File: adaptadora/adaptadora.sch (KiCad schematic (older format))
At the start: 39 parts, among them J1 Conn_Coaxial, J10 Conn_01x02, J11 Conn_Coaxial, J12 Conn_Coaxial, J2 Conn_Coaxial, J3 Conn_Coaxial, J4 Conn_Coaxial, J5 Conn_Coaxial, J6 Conn_01x02, J7 Conn_02x20_Odd_Even, J8 Conn_02x20_Odd_Even, J9 Conn_01x04, U1 LM361MX_NOPB-LM361MX_NOPB, U2 TLV2772IDR

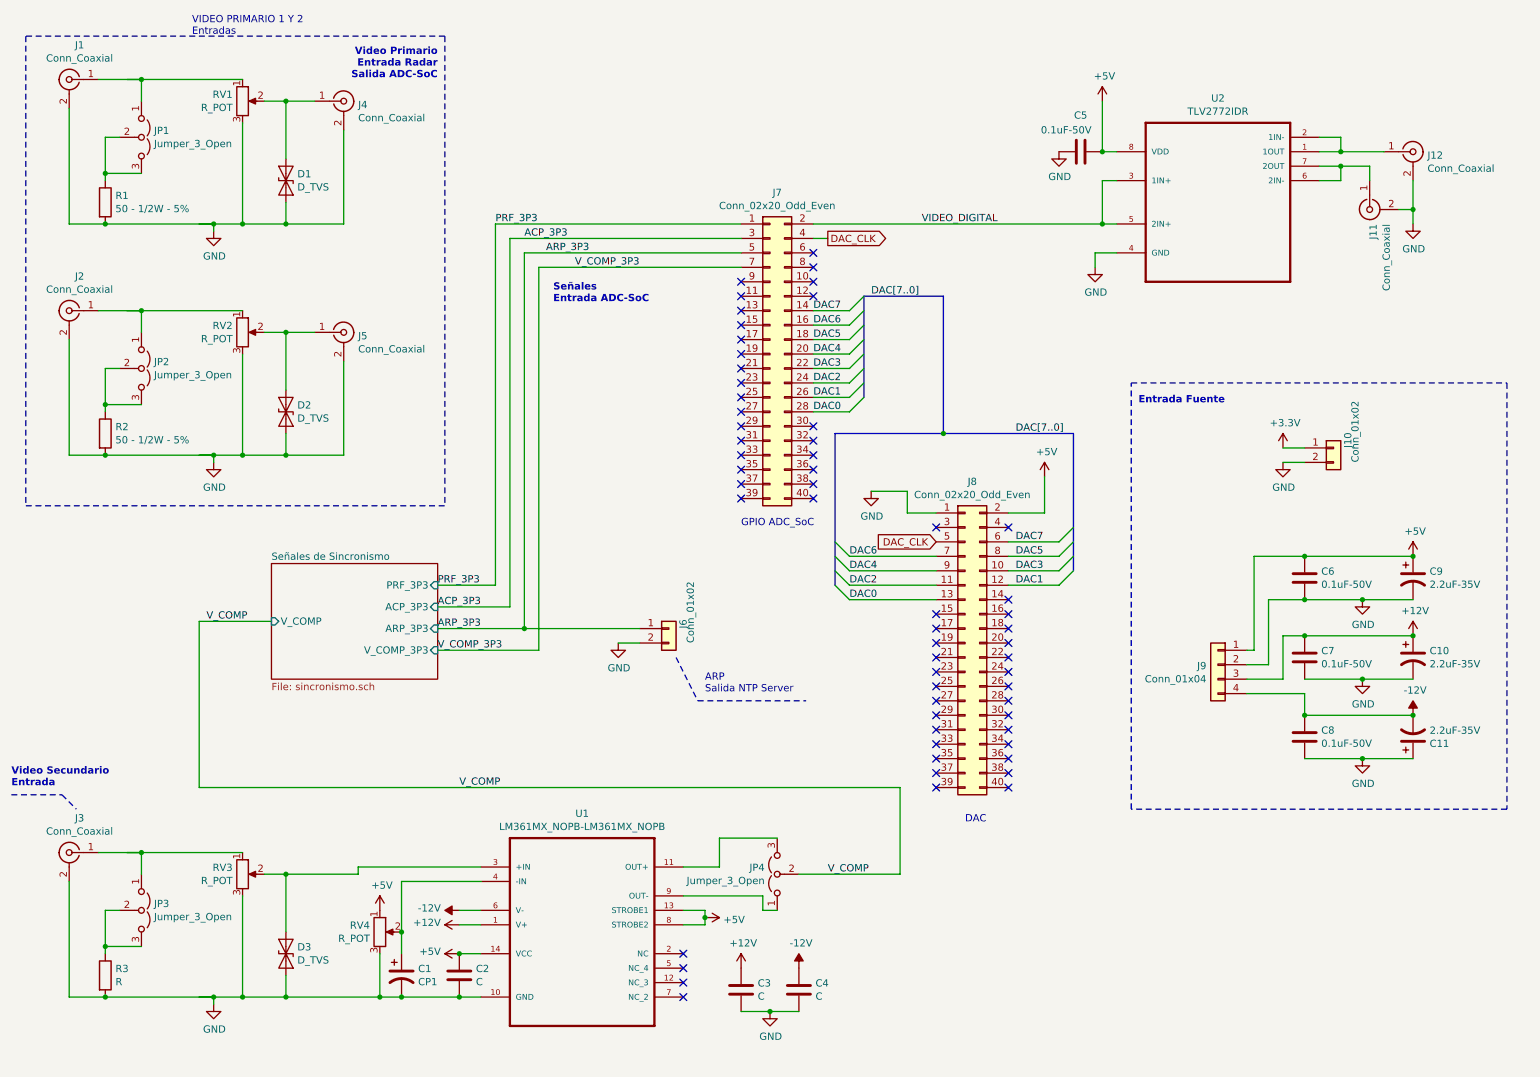
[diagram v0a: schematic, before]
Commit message: esquemático corregido por compañero
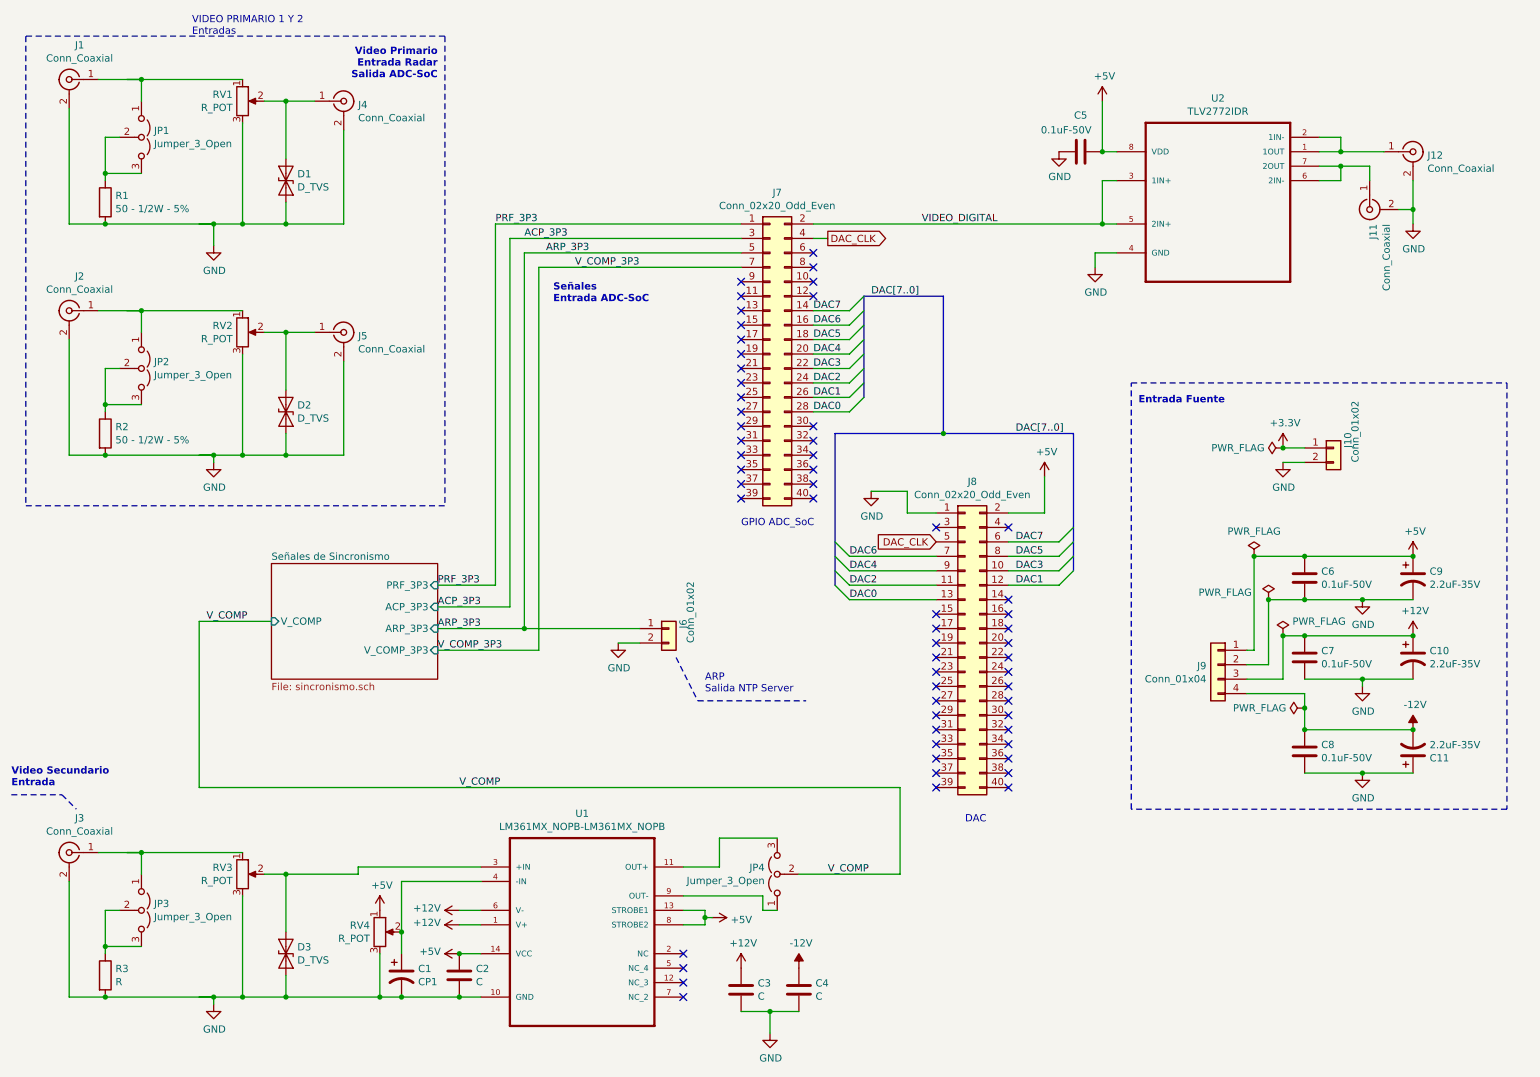
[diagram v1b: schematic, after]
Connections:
- wire segments 172 -> 176
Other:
- moved on the sheet: C11, C8

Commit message: work in progress
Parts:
- removed C1: CP1, symbol Device:CP1
- removed C2, C3, C4: C, symbol Device:C
- removed D3: D_TVS, symbol Device:D_TVS
- removed J3: Conn_Coaxial, symbol Connector:Conn_Coaxial
- removed JP3, JP4: Jumper_3_Open, symbol Jumper:Jumper_3_Open
- removed R3: R, symbol Device:R
- removed RV3, RV4: R_POT, symbol Device:R_POT
- removed U1: LM361MX_NOPB-LM361MX_NOPB, SOIC127P600X175-14N, symbol sincronismo-rescue:LM361MX_NOPB-LM361MX_NOPB
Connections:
- net labels removed: V_COMP
- wire segments 176 -> 124
- no-connect marks 59 -> 55
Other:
- note added: "Video Primario Digital\nSalida a otros equipos"
- note removed: "Video Secundario\nEntrada"
- moved on the sheet: D1, D2, J1, J11, J12, J2, J4, J5, J6, J7, J8, JP1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

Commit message: correcciones implementadas
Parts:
- U2_1: renamed from U2; Campo4 Texas Instruments -> (none); Campo5 Dual 2.7-V High Slew Rate Rail-To-Rail Output Operational A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 -> (none); Campo6 TLV2772IDR -> (none); Campo7 https://www.digikey.com/product-detail/en/texas-instruments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 -> (none); Campo8 SOIC-8 Texas Instruments -> (none); Descripción (inglés) (none) -> Dual 2.7-V High Slew Rate Rail-To-Rail Output Operational A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; Enlace (none) -> https://www.digikey.com/product-detail/en/texas-instruments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; Fabricante (none) -> Texas Instruments; Número de Parte (Digi-Key) (none) -> 296-1902-1-ND
- renumbered C5 to C1, C8 to C2, C11 to C3, C6 to C4, C7 to C5, C9 to C6, C10 to C7, J11 to J10, J12 to J11, J4 to J3, J5 to J4, J7 to J5, J8 to J7, J9 to J8, J10 to J9
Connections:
- wire segments 124 -> 130
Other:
- note added: "Señal de Video Secundario\nSeñal de Sincronismo de Rango\nEntradas ADC-SoC"
- note added: "Señales de sincronismo de Acimut\nEntrada ADC-SoC"
- note added: "U2_X: Amplificadores operacionales\nSalidas duplicadas para otros equipos\nTensión de salida: 5V"
- note removed: "Señales\nEntrada ADC-SoC"
- moved on the sheet: C2, C3, C4, C5, C6, C7, J7, J8, J9

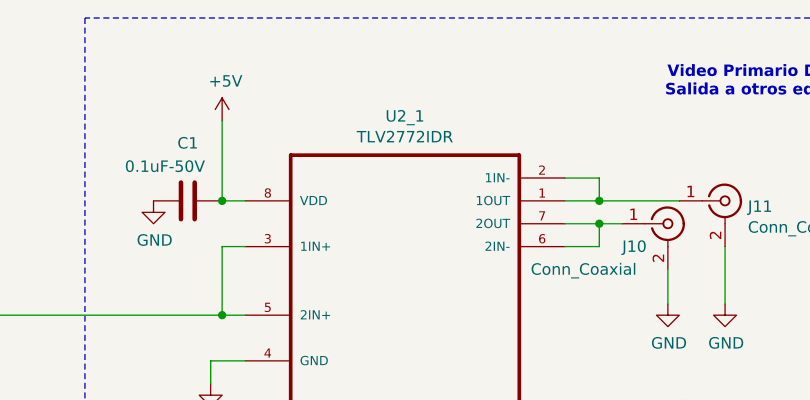
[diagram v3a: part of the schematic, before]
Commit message: se agregan huellas, en progreso
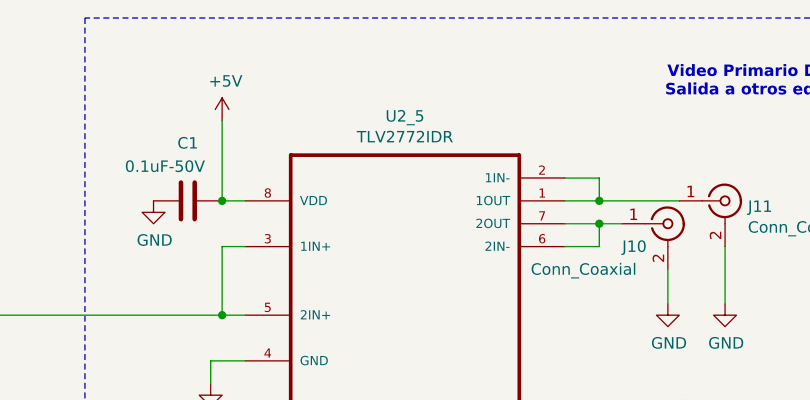
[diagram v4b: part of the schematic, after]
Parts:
- J1, J10, J11, J2, J3, J4: footprint (none) -> Connector_Coaxial:SMA_Amphenol_901-144_Vertical
- renumbered U2_1 to U2_5
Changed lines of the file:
@@
 F 0 "J1" H 1578 4388 50  0000 C CNN
 F 1 "Conn_Coaxial" H 1578 4297 50  0000 C CNN
-F 2 "" H 1650 4150 50  0001 C CNN
+F 2 "Connector_Coaxial:SMA_Amphenol_901-144_Vertical" H 1650 4150 50  0001 C CNN
 F 3 " ~" H 1650 4150 50  0001 C CNN
 	1    1650 4150
@@
 F 0 "J3" H 3650 4275 50  0000 L CNN
 F 1 "Conn_Coaxial" H 3650 4184 50  0000 L CNN
-F 2 "" H 3550 4300 50  0001 C CNN
+F 2 "Connector_Coaxial:SMA_Amphenol_901-144_Vertical" H 3550 4300 50  0001 C CNN
 F 3 " ~" H 3550 4300 50  0001 C CNN
 	1    3550 4300
@@
 F 0 "J2" H 1578 5988 50  0000 C CNN
 F 1 "Conn_Coaxial" H 1578 5897 50  0000 C CNN
-F 2 "" H 1650 5750 50  0001 C CNN
+F 2 "Connector_Coaxial:SMA_Amphenol_901-144_Vertical" H 1650 5750 50  0001 C CNN
 F 3 " ~" H 1650 5750 50  0001 C CNN
 	1    1650 5750
@@
 F 0 "J4" H 3650 5875 50  0000 L CNN
 F 1 "Conn_Coaxial" H 3650 5784 50  0000 L CNN
-F 2 "" H 3550 5900 50  0001 C CNN
+F 2 "Connector_Coaxial:SMA_Amphenol_901-144_Vertical" H 3550 5900 50  0001 C CNN
 F 3 " ~" H 3550 5900 50  0001 C CNN
 	1    3550 5900
@@
 F 0 "J10" H 9900 1400 50  0000 L CNN
 F 1 "Conn_Coaxial" H 9500 1300 50  0000 L CNN
-F 2 "" H 10100 1500 50  0001 C CNN
+F 2 "Connector_Coaxial:SMA_Amphenol_901-144_Vertical" H 10100 1500 50  0001 C CNN
 F 3 " ~" H 10100 1500 50  0001 C CNN
 	1    10100 1500
@@
 F 0 "J11" H 10450 1375 50  0000 L CNN
 F 1 "Conn_Coaxial" H 10450 1284 50  0000 L CNN
-F 2 "" H 10350 1400 50  0001 C CNN
+F 2 "Connector_Coaxial:SMA_Amphenol_901-144_Vertical" H 10350 1400 50  0001 C CNN
 F 3 " ~" H 10350 1400 50  0001 C CNN
 	1    10350 1400
@@
 $EndComp
 $Comp
-L TLV2772IDR:TLV2772IDR U2_1
+L TLV2772IDR:TLV2772IDR U2_5
 U 1 1 5DB05057
 P 8950 1600
-F 0 "U2_1" H 8950 2170 50  0000 C CNN
+F 0 "U2_5" H 8950 2170 50  0000 C CNN
 F 1 "TLV2772IDR" H 8950 2079 50  0000 C CNN
 F 2 "SOIC127P600X175-8N" H 8950 1150 50  0001 L BNN

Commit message: pcb work in progress
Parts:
- C1, C2, C4, C5: footprint (none) -> Capacitor_SMD:C_0805_2012Metric
- C3, C6, C7: footprint (none) -> Capacitor_Tantalum_SMD:CP_EIA-6032-28_Kemet-C
- D1, D2: footprint (none) -> Diode_THT:D_DO-15_P10.16mm_Horizontal
- J5: footprint (none) -> Connector_PinHeader_2.54mm:PinHeader_2x20_P2.54mm_Horizontal
- J6, J9: footprint (none) -> Connector_PinHeader_2.54mm:PinHeader_1x02_P2.54mm_Vertical
- J7: footprint (none) -> Connector_PinHeader_2.00mm:PinHeader_2x20_P2.00mm_Vertical
- J8: footprint (none) -> Connector_PinHeader_2.54mm:PinHeader_1x04_P2.54mm_Vertical
- JP1, JP2: footprint (none) -> Jumper:SolderJumper-3_P1.3mm_Open_Pad1.0x1.5mm_NumberLabels
- R1, R2: footprint (none) -> Resistor_THT:R_Axial_DIN0414_L11.9mm_D4.5mm_P15.24mm_Horizontal
- RV1, RV2: footprint (none) -> Potentiometer_THT:Potentiometer_Bourns_3296W_Vertical
- U25: renamed from U2_5; footprint SOIC127P600X175-8N -> Package_SO:SOIC-8_7.5x5.85mm_P1.27mm
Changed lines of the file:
@@
 F 0 "JP1" V 2104 4637 50  0000 L CNN
 F 1 "Jumper_3_Open" V 2195 4637 50  0000 L CNN
-F 2 "" H 2150 4550 50  0001 C CNN
+F 2 "Jumper:SolderJumper-3_P1.3mm_Open_Pad1.0x1.5mm_NumberLabels" H 2150 4550 50  0001 C CNN
 F 3 "~" H 2150 4550 50  0001 C CNN
 	1    2150 4550
@@
 F 0 "R1" H 1970 5046 50  0000 L CNN
 F 1 "50 - 1/2W - 5%" H 1970 4955 50  0000 L CNN
-F 2 "" V 1830 5000 50  0001 C CNN
+F 2 "Resistor_THT:R_Axial_DIN0414_L11.9mm_D4.5mm_P15.24mm_Horizontal" V 1830 5000 50  0001 C CNN
 F 3 "~" H 1900 5000 50  0001 C CNN
 	1    1900 5000
@@
 F 0 "RV1" H 2781 4346 50  0000 R CNN
 F 1 "R_POT" H 2781 4255 50  0000 R CNN
-F 2 "" H 2850 4300 50  0001 C CNN
+F 2 "Potentiometer_THT:Potentiometer_Bourns_3296W_Vertical" H 2850 4300 50  0001 C CNN
 F 3 "~" H 2850 4300 50  0001 C CNN
 	1    2850 4300
@@
 F 0 "D1" V 3104 4929 50  0000 L CNN
 F 1 "D_TVS" V 3195 4929 50  0000 L CNN
-F 2 "" H 3150 4850 50  0001 C CNN
+F 2 "Diode_THT:D_DO-15_P10.16mm_Horizontal" H 3150 4850 50  0001 C CNN
 F 3 "~" H 3150 4850 50  0001 C CNN
 	1    3150 4850
@@
 F 0 "JP2" V 2104 6237 50  0000 L CNN
 F 1 "Jumper_3_Open" V 2195 6237 50  0000 L CNN
-F 2 "" H 2150 6150 50  0001 C CNN
+F 2 "Jumper:SolderJumper-3_P1.3mm_Open_Pad1.0x1.5mm_NumberLabels" H 2150 6150 50  0001 C CNN
 F 3 "~" H 2150 6150 50  0001 C CNN
 	1    2150 6150
@@
 F 0 "R2" H 1970 6646 50  0000 L CNN
 F 1 "50 - 1/2W - 5%" H 1970 6555 50  0000 L CNN
-F 2 "" V 1830 6600 50  0001 C CNN
+F 2 "Resistor_THT:R_Axial_DIN0414_L11.9mm_D4.5mm_P15.24mm_Horizontal" V 1830 6600 50  0001 C CNN
 F 3 "~" H 1900 6600 50  0001 C CNN
 	1    1900 6600
@@
 F 0 "RV2" H 2781 5946 50  0000 R CNN
 F 1 "R_POT" H 2781 5855 50  0000 R CNN
-F 2 "" H 2850 5900 50  0001 C CNN
+F 2 "Potentiometer_THT:Potentiometer_Bourns_3296W_Vertical" H 2850 5900 50  0001 C CNN
 F 3 "~" H 2850 5900 50  0001 C CNN
 	1    2850 5900
@@
 F 0 "D2" V 3104 6529 50  0000 L CNN
 F 1 "D_TVS" V 3195 6529 50  0000 L CNN
-F 2 "" H 3150 6450 50  0001 C CNN
+F 2 "Diode_THT:D_DO-15_P10.16mm_Horizontal" H 3150 6450 50  0001 C CNN
 F 3 "~" H 3150 6450 50  0001 C CNN
 	1    3150 6450
@@
 ARP_3P3
 $Comp
-L Connector_Generic:Conn_02x20_Odd_Even J5
-U 1 1 5D77C6C1
-P 5100 2800
-F 0 "J5" H 5150 3917 50  0000 C CNN
-F 1 "Conn_02x20_Odd_Even" H 5150 3826 50  0000 C CNN
-F 2 "" H 5100 2800 50  0001 C CNN
-F 3 "~" H 5100 2800 50  0001 C CNN
-	1    5100 2800
-	1    0    0    -1
-$EndComp
-$Comp
 L Connector:Conn_Coaxial J10
 U 1 1 5DB05046
@@
 $EndComp
 $Comp
-L TLV2772IDR:TLV2772IDR U2_5
+L TLV2772IDR:TLV2772IDR U25
 U 1 1 5DB05057
 P 8950 1600
-F 0 "U2_5" H 8950 2170 50  0000 C CNN
+F 0 "U25" H 8950 2170 50  0000 C CNN
 F 1 "TLV2772IDR" H 8950 2079 50  0000 C CNN
-F 2 "SOIC127P600X175-8N" H 8950 1150 50  0001 L BNN
+F 2 "Package_SO:SOIC-8_7.5x5.85mm_P1.27mm" H 8950 1150 50  0001 L BNN
 F 3 "296-1902-1-ND" H 8950 1150 50  0001 L BNN
 F 4 "Texas Instruments" H 8950 1150 50  0001 L BNN "Fabricante"
@@
 F 0 "C1" V 7748 1400 50  0000 C CNN
 F 1 "0.1uF-50V" V 7850 1300 50  0000 C CNN
-F 2 "" H 8038 1250 50  0001 C CNN
+F 2 "Capacitor_SMD:C_0805_2012Metric" H 8038 1250 50  0001 C CNN
 F 3 "~" H 8000 1400 50  0001 C CNN
 	1    8000 1400
@@
 F 0 "J7" H 6150 6817 50  0000 C CNN
 F 1 "Conn_02x20_Odd_Even" H 6150 6726 50  0000 C CNN
-F 2 "" H 6100 5700 50  0001 C CNN
+F 2 "Connector_PinHeader_2.00mm:PinHeader_2x20_P2.00mm_Vertical" H 6100 5700 50  0001 C CNN
 F 3 "~" H 6100 5700 50  0001 C CNN
 	1    6100 5700
@@
 Wire Wire Line
 	5400 2600 5650 2600
-Wire Wire Line
-	5400 2700 5650 2700
-Wire Wire Line
-	5400 2800 5650 2800
-Wire Wire Line
-	5400 2900 5650 2900
-Wire Wire Line
-	5400 3000 5650 3000
-Wire Wire Line
-	5400 3100 5650 3100
-Wire Wire Line
-	5400 3200 5650 3200
-Text Label 5400 3200 0    50   ~ 0
-DAC0
-Text Label 5400 3100 0    50   ~ 0
-DAC1
-Text Label 5400 3000 0    50   ~ 0
-DAC2
-Text Label 5400 2900 0    50   ~ 0
-DAC3
-Text Label 5400 2800 0    50   ~ 0
-DAC4
-Text Label 5400 2700 0    50   ~ 0
-DAC5
 Text Label 5400 2600 0    50   ~ 0
 DAC6
 Text Label 5400 2500 0    50   ~ 0
 DAC7
-Entry Wire Line
-	5650 3200 5750 3100
-Entry Wire Line
-	5650 3100 5750 3000
-Entry Wire Line
-	5650 3000 5750 2900
-Entry Wire Line
-	5650 2900 5750 2800
-Entry Wire Line
-	5650 2800 5750 2700
-Entry Wire Line
-	5650 2700 5750 2600
 Entry Wire Line
 	5650 2600 5750 2500
@@
 NoConn ~ 4900 3400
 NoConn ~ 4900 3300
-NoConn ~ 4900 3200
-NoConn ~ 4900 3100
-NoConn ~ 4900 3000
-NoConn ~ 4900 2900
-NoConn ~ 4900 2800
-NoConn ~ 4900 2700
 NoConn ~ 4900 2600
 NoConn ~ 4900 2500
@@
 Wire Wire Line
 	3600 1400 2650 1400
-Wire Wire Line
-	3600 2000 4900 2000
 Text Label 2950 2650 0    50   ~ 0
 PRF_3P3
@@
 F 0 "J6" V 5700 850 50  0000 L CNN
 F 1 "Conn_01x02" V 5800 700 50  0000 L CNN
-F 2 "" H 5550 950 50  0001 C CNN
+F 2 "Connector_PinHeader_2.54mm:PinHeader_1x02_P2.54mm_Vertical" H 5550 950 50  0001 C CNN
 F 3 "~" H 5550 950 50  0001 C CNN
 	1    5550 950
@@
 F 0 "J9" V 9550 3350 50  0000 L CNN
 F 1 "Conn_01x02" V 9650 3200 50  0000 L CNN
-F 2 "" H 9400 3450 50  0001 C CNN
+F 2 "Connector_PinHeader_2.54mm:PinHeader_1x02_P2.54mm_Vertical" H 9400 3450 50  0001 C CNN
 F 3 "~" H 9400 3450 50  0001 C CNN
 	1    9400 3450
@@
 F 0 "C7" H 10415 4846 50  0000 L CNN
 F 1 "2.2uF-35V" H 10415 4755 50  0000 L CNN
-F 2 "" H 10300 4800 50  0001 C CNN
+F 2 "Capacitor_Tantalum_SMD:CP_EIA-6032-28_Kemet-C" H 10300 4800 50  0001 C CNN
 F 3 "~" H 10300 4800 50  0001 C CNN
 	1    10300 4800
@@
 F 0 "C6" H 10415 4296 50  0000 L CNN
 F 1 "2.2uF-35V" H 10415 4205 50  0000 L CNN
-F 2 "" H 10300 4250 50  0001 C CNN
+F 2 "Capacitor_Tantalum_SMD:CP_EIA-6032-28_Kemet-C" H 10300 4250 50  0001 C CNN
 F 3 "~" H 10300 4250 50  0001 C CNN
 	1    10300 4250
@@
 F 0 "C2" H 9165 5546 50  0000 L CNN
 F 1 "0.1uF-50V" H 9165 5455 50  0000 L CNN
-F 2 "" H 9088 5350 50  0001 C CNN
+F 2 "Capacitor_SMD:C_0805_2012Metric" H 9088 5350 50  0001 C CNN
 F 3 "~" H 9050 5500 50  0001 C CNN
 	1    9050 5500
@@
 F 0 "C5" H 9665 4846 50  0000 L CNN
 F 1 "0.1uF-50V" H 9665 4755 50  0000 L CNN
-F 2 "" H 9588 4650 50  0001 C CNN
+F 2 "Capacitor_SMD:C_0805_2012Metric" H 9588 4650 50  0001 C CNN
 F 3 "~" H 9550 4800 50  0001 C CNN
 	1    9550 4800
@@
 F 0 "C4" H 9665 4296 50  0000 L CNN
 F 1 "0.1uF-50V" H 9665 4205 50  0000 L CNN
-F 2 "" H 9588 4100 50  0001 C CNN
+F 2 "Capacitor_SMD:C_0805_2012Metric" H 9588 4100 50  0001 C CNN
 F 3 "~" H 9550 4250 50  0001 C CNN
 	1    9550 4250
@@
 F 0 "J8" H 8830 4842 50  0000 L CNN
 F 1 "Conn_01x04" H 8830 4751 50  0000 L CNN
-F 2 "" H 8750 4850 50  0001 C CNN
+F 2 "Connector_PinHeader_2.54mm:PinHeader_1x04_P2.54mm_Vertical" H 8750 4850 50  0001 C CNN
 F 3 "~" H 8750 4850 50  0001 C CNN
 	1    8750 4850
@@
 F 0 "C3" H 9165 5896 50  0000 L CNN
 F 1 "2.2uF-35V" H 9165 5805 50  0000 L CNN
-F 2 "" H 9050 5850 50  0001 C CNN
+F 2 "Capacitor_Tantalum_SMD:CP_EIA-6032-28_Kemet-C" H 9050 5850 50  0001 C CNN
 F 3 "~" H 9050 5850 50  0001 C CNN
 	1    9050 5850
@@
 $EndComp
 Wire Wire Line
-	4900 2200 3800 2200
-Wire Wire Line
 	9050 6050 8700 6050
 Wire Wire Line
@@
 Wire Wire Line
 	9050 6050 9050 6100
-Wire Wire Line
-	4900 2100 3600 2100
 Wire Wire Line
 	3600 2100 3600 2650
@@
 Wire Bus Line
 	5200 4250 5200 5300
+Wire Wire Line
+	4900 2200 3800 2200
+Wire Wire Line
+	4900 2100 3600 2100
+Wire Wire Line
+	3600 2000 4900 2000
 Wire Bus Line
 	5750 2400 5750 3100
+NoConn ~ 4900 2700
+NoConn ~ 4900 2800
+NoConn ~ 4900 2900
+NoConn ~ 4900 3000
+NoConn ~ 4900 3100
+NoConn ~ 4900 3200
+Entry Wire Line
+	5650 2700 5750 2600
+Entry Wire Line
+	5650 2800 5750 2700
+Entry Wire Line
+	5650 2900 5750 2800
+Entry Wire Line
+	5650 3000 5750 2900
+Entry Wire Line
+	5650 3100 5750 3000
+Entry Wire Line
+	5650 3200 5750 3100
+Text Label 5400 2700 0    50   ~ 0
+DAC5
+Text Label 5400 2800 0    50   ~ 0
+DAC4
+Text Label 5400 2900 0    50   ~ 0
+DAC3
+Text Label 5400 3000 0    50   ~ 0
+DAC2
+Text Label 5400 3100 0    50   ~ 0
+DAC1
+Text Label 5400 3200 0    50   ~ 0
+DAC0
+Wire Wire Line
+	5400 3200 5650 3200
+Wire Wire Line
+	5400 3100 5650 3100
+Wire Wire Line
+	5400 3000 5650 3000
+Wire Wire Line
+	5400 2900 5650 2900
+Wire Wire Line
+	5400 2800 5650 2800
+Wire Wire Line
+	5400 2700 5650 2700
+$Comp
+L Connector_Generic:Conn_02x20_Odd_Even J5
+U 1 1 5D77C6C1
+P 5100 2800
+F 0 "J5" H 5150 3917 50  0000 C CNN
+F 1 "Conn_02x20_Odd_Even" H 5150 3826 50  0000 C CNN
+F 2 "Connector_PinHeader_2.54mm:PinHeader_2x20_P2.54mm_Horizontal" H 5100 2800 50  0001 C CNN
+F 3 "~" H 5100 2800 50  0001 C CNN
+	1    5100 2800
+	1    0    0    -1
+$EndComp
 $EndSCHEMATC
